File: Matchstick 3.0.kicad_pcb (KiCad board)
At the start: 2 copper layers, 60.2 x 34 mm, 11 parts, among them J3 Barrel_Jack, J4 Screw_Terminal_01x08, SW1 SparkFun_COM-08720, U3 M5StampS3

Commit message: updated sch+pcb
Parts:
- removed H1, H2: MountingHole, MountingHole:MountingHole_3.5mm
- removed U3: M5StampS3, M5Stack_SMD:M5StampS3
- added U1: M5StampS3, M5Stack_SMD:M5StampS3, B.Cu at (184.0, 107.5)
- J3: footprint Connector_Custom:BarrelJack_Horizontal_Custom -> Connector_BarrelJack:BarrelJack_Horizontal
- SW1: footprint Switch_SMD:SparkFun_COM-08720 -> SparkFun:SparkFun_COM-08720
- moved SW1 41.6 mm to (163.2, 95.1), turned to 90 degrees
- moved D1 26.5 mm to (168.6, 115.5)
- moved R1 26.5 mm to (165.6, 115.4)
- moved C2 26.3 mm to (179.9, 112.2), turned to 0 degrees
- moved J4 13.2 mm to (200.8, 116.8)
- moved C1 12.6 mm to (193.4, 105.4), turned to 180 degrees
- moved U2 12.1 mm to (193.3, 111.1), turned to 0 degrees
- moved J3 0.99 mm to (170.0, 104.5)
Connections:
- U2 pad 11: CLK2 -> CLK1
- U2 pad 3: CLK1 -> CLK2
- U2 pad 6: DATA1 -> DATA2
- U2 pad 8: DATA2 -> DATA1
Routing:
- net +5V: track 41.3 -> 106.2 mm
- net CLK2: track 1.75 -> 30.1 mm
- net GND: track 25.7 -> 45.7 mm, vias 0 -> 1
- net DATA2: track 2.02 -> 19.9 mm
- net unconnected-(D1-A-Pad2): track 1.78 -> 10.8 mm, vias 0 -> 1
- net C2: track 1.98 -> 10.9 mm, vias 0 -> 1
- net CLK1: track 14.5 -> 5.54 mm
- net C1: track 1.44 -> 9.07 mm, vias 0 -> 1
- net unconnected-(SW1-Pad1): track 28.2 -> 35.5 mm, vias 0 -> 1
- net D2: track 2.88 -> 9.55 mm, vias 0 -> 1
- net D1: track 2.11 -> 7.74 mm, vias 0 -> 1
- net DATA1: track 9.22 -> 5.67 mm
- removed copper zone on B.Cu, net GND
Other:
- board size 60.2 x 34 mm -> 47.2 x 34 mm

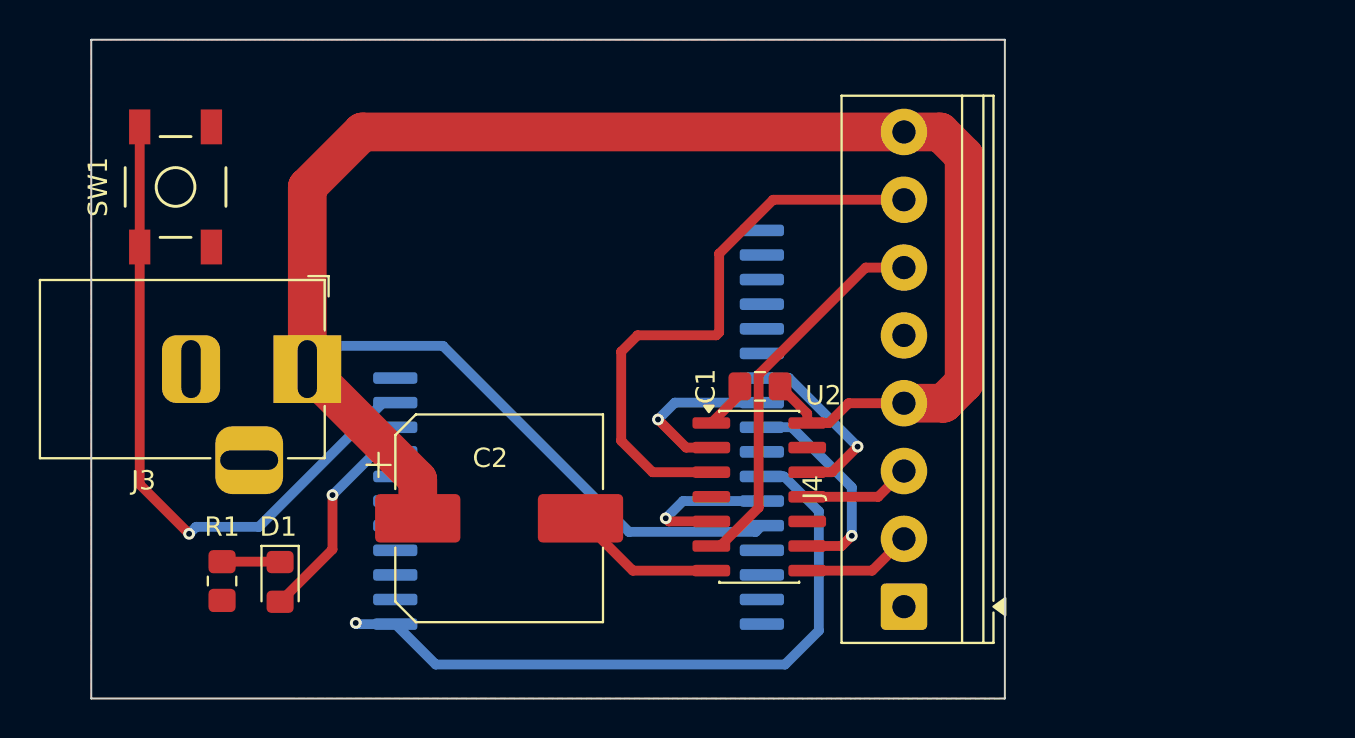
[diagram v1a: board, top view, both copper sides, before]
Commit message: fixed ground planes
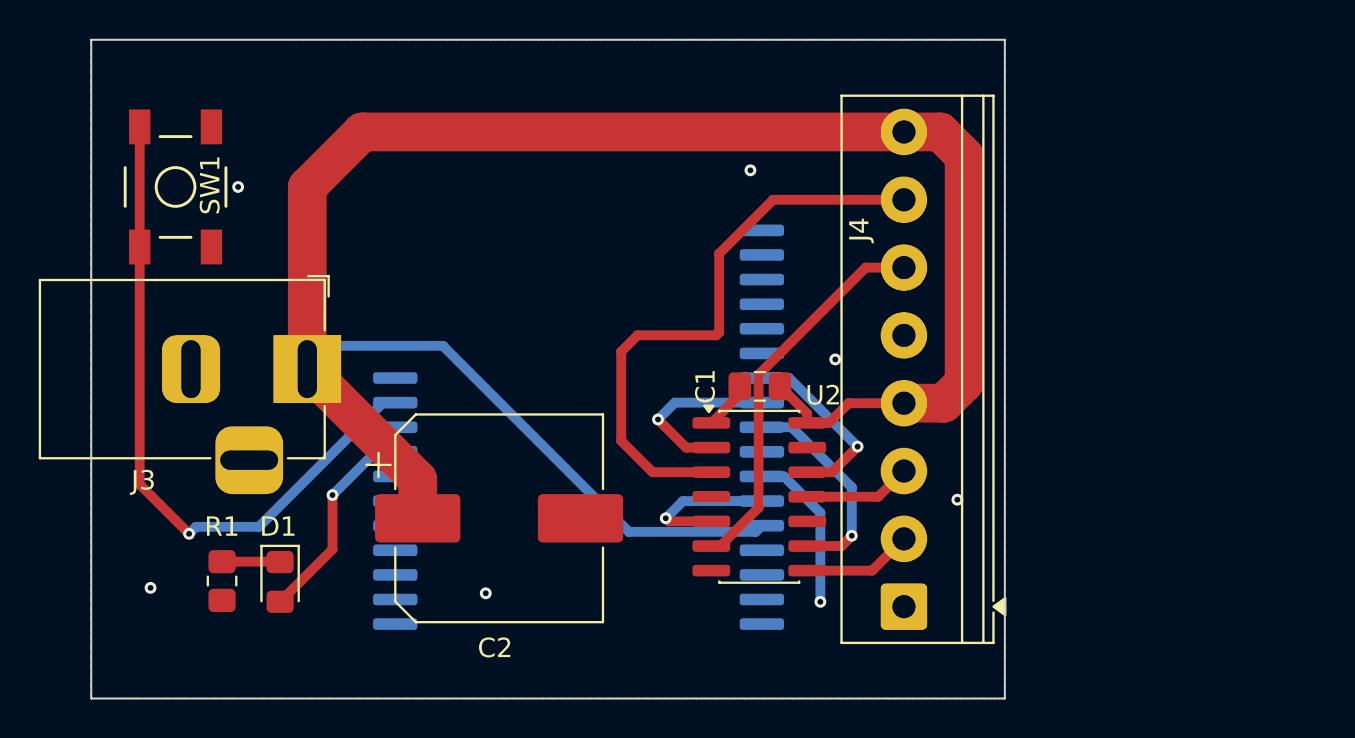
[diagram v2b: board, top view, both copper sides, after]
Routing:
- net GND: track 45.7 -> 10.9 mm, vias 1 -> 7
- added copper zone on B.Cu, net GND
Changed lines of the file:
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@@
 		(tags "THT Terminal Block Phoenix PT-1,5-8-3.5-H pitch 3.5mm size 28x7.6mm drill 1.2mm pad 2.4mm")
 		(property "Reference" "J4"
-			(at 6.16 -4.7 90)
+			(at 19.46 -2.292893 90)
 			(layer "F.SilkS")
 			(effects
@@
 		(tags "capacitor electrolytic")
 		(property "Reference" "C2"
-			(at -0.46 -3.11 0)
+			(at -0.2 6.7 0)
 			(layer "F.SilkS")
 			(effects
@@
 		(tags "Pushbutton Switch COM-08720")
 		(property "Reference" "SW1"
-			(at 0 -4 90)
+			(at 0.1 1.8 90)
 			(unlocked yes)
 			(layer "F.SilkS")
@@
 	)
 	(segment
-		(start 186.8 114.9)
-		(end 190.85 114.9)
-		(width 0.508)
-		(layer "F.Cu")
-		(net 2)
-	)
-	(segment
 		(start 192.325 105.39)
 		(end 192.325 105.805)
@@
 	)
 	(segment
-		(start 184.1 112.2)
-		(end 186.8 114.9)
-		(width 0.508)
-		(layer "F.Cu")
-		(net 2)
-	)
-	(segment
 		(start 192.325 105.805)
 		(end 190.85 107.28)
@@
 	)
 	(via
-		(at 172.5 117.6)
+		(at 192.87 94.24)
 		(size 0.61)
 		(drill 0.3)
 		(layers "F.Cu" "B.Cu")
+		(free yes)
 		(net 2)
 	)
-	(segment
-		(start 176.625 119.745)
-		(end 174.54 117.66)
+	(via
+		(at 196.48 116.51)
+		(size 0.61)
+		(drill 0.3)
+		(layers "F.Cu" "B.Cu")
+		(free yes)
+		(net 2)
+	)
+	(via
+		(at 197.25 104)
+		(size 0.61)
+		(drill 0.3)
+		(layers "F.Cu" "B.Cu")
+		(free yes)
+		(net 2)
+	)
+	(via
+		(at 203.55 111.24)
+		(size 0.61)
+		(drill 0.3)
+		(layers "F.Cu" "B.Cu")
+		(free yes)
+		(net 2)
+	)
+	(via
+		(at 179.21 116.07)
+		(size 0.61)
+		(drill 0.3)
+		(layers "F.Cu" "B.Cu")
+		(free yes)
+		(net 2)
+	)
+	(via
+		(at 161.91 115.79)
+		(size 0.61)
+		(drill 0.3)
+		(layers "F.Cu" "B.Cu")
+		(free yes)
+		(net 2)
+	)
+	(via
+		(at 166.43 95.1)
+		(size 0.61)
+		(drill 0.3)
+		(layers "F.Cu" "B.Cu")
+		(free yes)
+		(net 2)
+	)
+	(segment
+		(start 196.48 111.917001)
+		(end 196.48 116.51)
 		(width 0.508)
 		(layer "B.Cu")
@@
 	)
 	(segment
-		(start 196.4 111.837001)
-		(end 196.4 118)
+		(start 194.602999 110.04)
+		(end 196.48 111.917001)
 		(width 0.508)
 		(layer "B.Cu")
@@
 	)
 	(segment
-		(start 194.655 119.745)
-		(end 176.625 119.745)
-		(width 0.508)
-		(layer "B.Cu")
-		(net 2)
-	)
-	(segment
-		(start 194.602999 110.04)
-		(end 196.4 111.837001)
-		(width 0.508)
-		(layer "B.Cu")
-		(net 2)
-	)
-	(segment
 		(start 193.46 110.04)
 		(end 194.602999 110.04)
-		(width 0.508)
-		(layer "B.Cu")
-		(net 2)
-	)
-	(segment
-		(start 172.56 117.66)
-		(end 172.5 117.6)
-		(width 0.508)
-		(layer "B.Cu")
-		(net 2)
-	)
-	(segment
-		(start 196.4 118)
-		(end 194.655 119.745)
-		(width 0.508)
-		(layer "B.Cu")
-		(net 2)
-	)
-	(segment
-		(start 174.54 117.66)
-		(end 172.56 117.66)
 		(width 0.508)
 		(layer "B.Cu")
@@
 		(layer "F.Cu")
 		(hatch edge 0.5)
-		(priority 1)
 		(connect_pads
 			(clearance 0)
@@
 		(polygon
 			(pts
-				(xy 158.85 87.5) (xy 206 87.5) (xy 206 121.5) (xy 158.85 121.5)
+				(xy 158.85 87.5) (xy 158.85 121.5) (xy 205.998318 121.514769) (xy 205.998318 87.514769)
 			)
 		)
@@
 		(net 2)
 		(net_name "GND")
-		(layer "F.Cu")
+		(layers "F.Cu" "B.Cu")
 		(hatch edge 0.5)
+		(priority 1)
 		(connect_pads
-			(clearance 0)
+			(clearance 0.1)
 		)
 		(min_thickness 0.25)
@@
 		(polygon
 			(pts
-				(xy 158.85 87.5) (xy 158.85 121.5) (xy 205.998318 121.514769) (xy 205.998318 87.514769)
-			)
-		)
+				(xy 158.85 87.5) (xy 206 87.5) (xy 206 121.5) (xy 158.85 121.5)
+			)
+		)

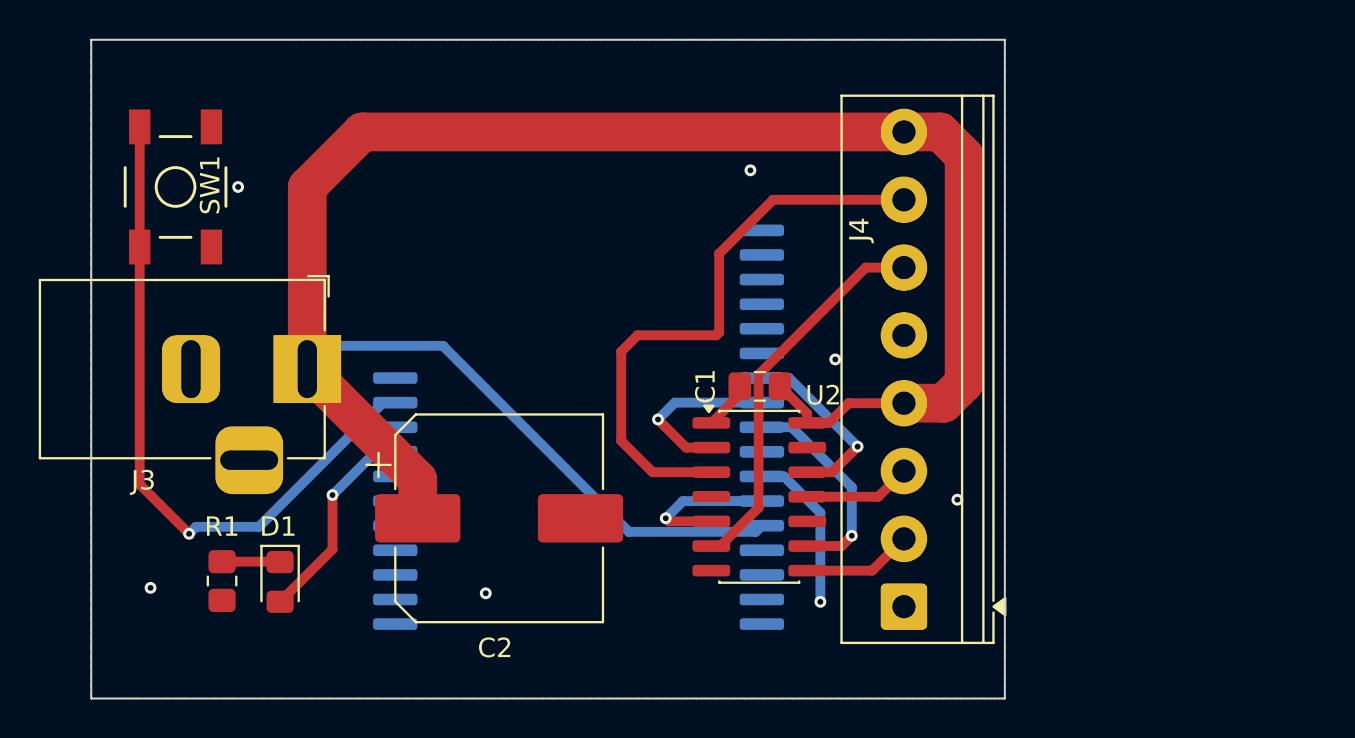
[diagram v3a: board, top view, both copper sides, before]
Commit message: fixed spacing and ERC and DRC errors
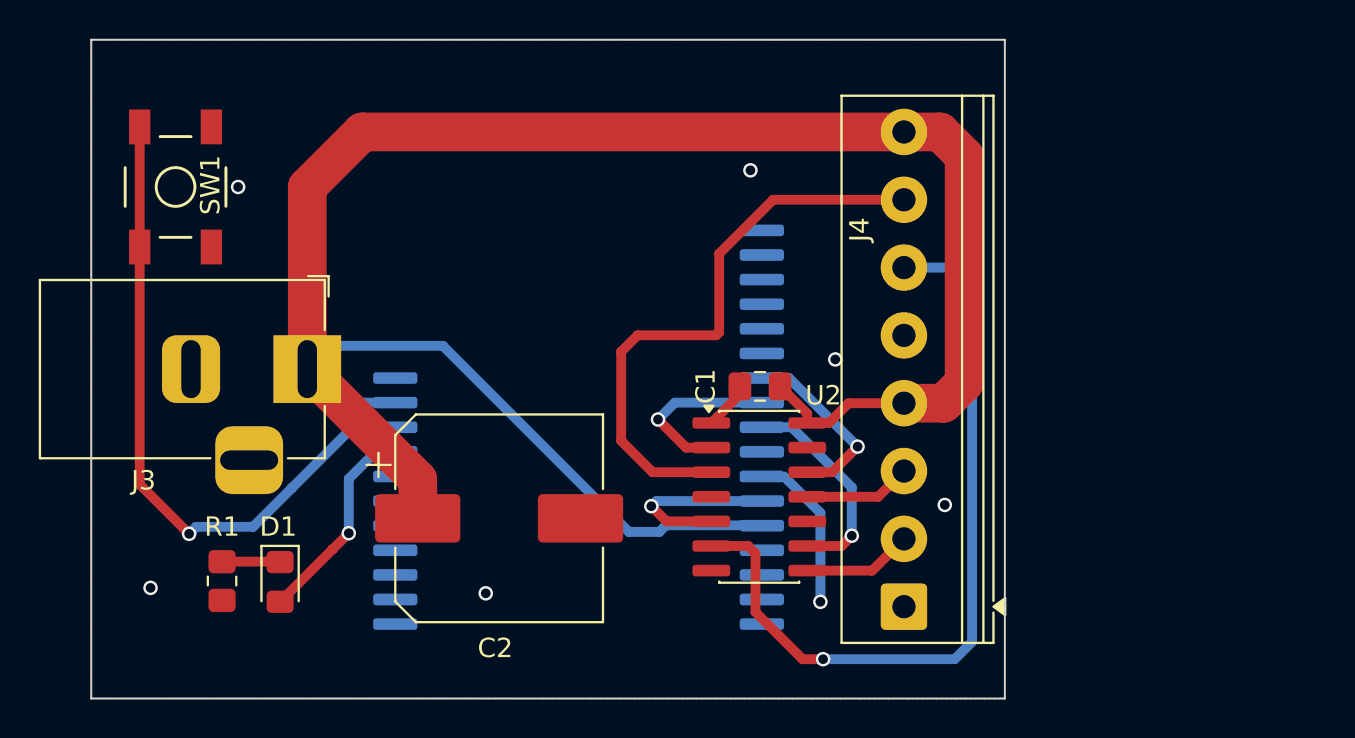
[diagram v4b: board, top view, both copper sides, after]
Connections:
- net Net-(D1-K) renamed /LED2
- D1 pad 2: unconnected-(D1-A-Pad2) -> /LED
- SW1 pad 1: unconnected-(SW1-Pad1) -> /SW1
- U1 pad 25: unconnected-(D1-A-Pad2) -> /LED
- U1 pad 27: unconnected-(SW1-Pad1) -> /SW1
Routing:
- net unconnected-(SW1-Pad1): track 35.5 -> 0.00 mm, vias 1 -> 0
- net /SW1: track 0.00 -> 35.0 mm, vias 0 -> 1
- net DATA2: track 19.9 -> 40.1 mm, vias 0 -> 1
- net /LED: track 0.00 -> 10.8 mm, vias 0 -> 1
- net unconnected-(D1-A-Pad2): track 10.8 -> 0.00 mm, vias 1 -> 0
- net D1: track 7.74 -> 9.23 mm
- net GND: track 10.9 -> 9.75 mm

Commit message: silkscreen logo
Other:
- board text added: "+5V +5V"
- board text added: "0x76656E Labs"
- board text added: "C1 G08"
- board text added: "C2 G09"
- board text added: "D1 G12"
- board text added: "D2 G07"
- board text added: "GND GND"
- board text added: "MATCH STICK 0x03"
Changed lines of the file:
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@@
 		(tags "capacitor handsolder")
 		(property "Reference" "C1"
-			(at 2.8 0 90)
+			(at 2.9325 0.06 180)
 			(layer "F.SilkS")
 			(effects
@@
 		(tags "SOIC SO")
 		(property "Reference" "U2"
-			(at 3.31 -5.23 0)
+			(at -2.015 5.61 0)
 			(layer "F.SilkS")
 			(effects
@@
 		(embedded_fonts no)
 	)
+	(gr_rect
+		(start 172.818554 87.57)
+		(end 194.451447 102.91)
+		(stroke
+			(width 0.15)
+			(type solid)
+		)
+		(fill yes)
+		(layer "F.SilkS")
+	)
 	(gr_line
 		(start 158.85 87.5)
@@
 		(layer "Edge.Cuts")
 	)
+	(gr_text "+5V     +5V"
+		(at 206.08 106.98 0)
+		(layer "B.SilkS" knockout)
+		(effects
+			(font
+				(size 1.25 1)
+				(thickness 0.15)
+				(bold yes)
+			)
+			(justify left bottom mirror)
+		)
+	)
+	(gr_text "C1       G08"
+		(at 206.03 110.54 0)
+		(layer "B.SilkS" knockout)
+		(effects
+			(font
+				(size 1.25 1)
+				(thickness 0.15)
+				(bold yes)
+			)
+			(justify left bottom mirror)
+		)
+	)
+	(gr_text "MATCH\nSTICK\n0x03"
+		(at 160.02 96.02 0)
+		(layer "B.SilkS" knockout)
+		(effects
+			(font
+				(size 1.5 1.5)
+				(thickness 0.375)
+				(bold yes)
+			)
+			(justify right bottom mirror)
+		)
+	)
+	(gr_text "GND     GND"
+		(at 206.05 103.55 0)
+		(layer "B.SilkS" knockout)
+		(effects
+			(font
+				(size 1.25 1)
+				(thickness 0.15)
+				(bold yes)
+			)
+			(justify left bottom mirror)
+		)
+	)
+	(gr_text "GND     GND"
+		(at 206.03 117.49 0)
+		(layer "B.SilkS" knockout)
+		(effects
+			(font
+				(size 1.25 1)
+				(thickness 0.15)
+				(bold yes)
+			)
+			(justify left bottom mirror)
+		)
+	)
+	(gr_text "D2       G07"
+		(at 206.1 100 0)
+		(layer "B.SilkS" knockout)
+		(effects
+			(font
+				(size 1.25 1)
+				(thickness 0.15)
+				(bold yes)
+			)
+			(justify left bottom mirror)
+		)
+	)
+	(gr_text "C2       G09\n"
+		(at 206.05 96.6 0)
+		(layer "B.SilkS" knockout)
+		(effects
+			(font
+				(size 1.25 1)
+				(thickness 0.15)
+				(bold yes)
+			)
+			(justify left bottom mirror)
+		)
+	)
+	(gr_text "D1       G12"
+		(at 206.08 113.95 0)
+		(layer "B.SilkS" knockout)
+		(effects
+			(font
+				(size 1.25 1)
+				(thickness 0.15)
+				(bold yes)
+			)
+			(justify left bottom mirror)
+		)
+	)
+	(gr_text "+5V     +5V"
+		(at 206.1 93.04 0)
+		(layer "B.SilkS" knockout)
+		(effects
+			(font
+				(size 1.25 1)
+				(thickness 0.15)
+				(bold yes)
+			)
+			(justify left bottom mirror)
+		)
+	)
+	(gr_text "0x76656E\nLabs"
+		(at 160.21 99.94 0)
+		(layer "B.SilkS")
+		(effects
+			(font
+				(size 1 0.98)
+				(thickness 0.15)
+				(bold yes)
+			)
+			(justify right bottom mirror)
+		)
+	)
 	(segment

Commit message: fixed the nets, and connections
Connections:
- U1 pad 12: D1 -> D2
- U1 pad 7: D2 -> C1
- U1 pad 8: C1 -> C2
- U1 pad 9: C2 -> D1
- U2 pad 12: D2 -> C1
- U2 pad 2: C1 -> C2
- U2 pad 5: D1 -> D2
- U2 pad 9: C2 -> D1
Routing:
- net C2: track 10.9 -> 9.07 mm
- net D1: track 9.23 -> 10.9 mm
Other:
- board text added: "C1 G07"
- board text added: "C2 G08"
- board text added: "D1 G09"
- board text added: "D2 G11"
- board text removed: "C1 G08"
- board text removed: "C2 G09"
- board text removed: "D1 G12"
- board text removed: "D2 G07"
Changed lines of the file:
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@@
 			(layers "F.Cu" "F.Mask" "F.Paste")
 			(roundrect_rratio 0.25)
-			(net 11 "C1")
+			(net 9 "C2")
 			(pinfunction "A")
 			(pintype "input")
@@
 			(layers "F.Cu" "F.Mask" "F.Paste")
 			(roundrect_rratio 0.25)
-			(net 8 "D1")
+			(net 10 "D2")
 			(pinfunction "A")
 			(pintype "input")
@@
 			(layers "F.Cu" "F.Mask" "F.Paste")
 			(roundrect_rratio 0.25)
-			(net 9 "C2")
+			(net 8 "D1")
 			(pinfunction "A")
 			(pintype "input")
@@
 			(layers "F.Cu" "F.Mask" "F.Paste")
 			(roundrect_rratio 0.25)
-			(net 10 "D2")
+			(net 11 "C1")
 			(pinfunction "A")
 			(pintype "input")
@@
 			(layers "B.Cu" "B.Mask" "B.Paste")
 			(roundrect_rratio 0.25)
-			(net 10 "D2")
+			(net 11 "C1")
 			(pinfunction "G7")
 			(pintype "bidirectional")
@@
 			(layers "B.Cu" "B.Mask" "B.Paste")
 			(roundrect_rratio 0.25)
-			(net 11 "C1")
+			(net 9 "C2")
 			(pinfunction "G8")
 			(pintype "bidirectional")
@@
 			(layers "B.Cu" "B.Mask" "B.Paste")
 			(roundrect_rratio 0.25)
-			(net 9 "C2")
+			(net 8 "D1")
 			(pinfunction "G9")
 			(pintype "bidirectional")
@@
 			(layers "B.Cu" "B.Mask" "B.Paste")
 			(roundrect_rratio 0.25)
-			(net 8 "D1")
+			(net 10 "D2")
 			(pinfunction "G11")
 			(pintype "bidirectional")
@@
 		(layer "F.SilkS")
 	)
+	(gr_rect
+		(start 160.25 89.07)
+		(end 167.43 99.49)
+		(stroke
+			(width 0.15)
+			(type default)
+		)
+		(fill no)
+		(layer "B.SilkS")
+	)
 	(gr_line
 		(start 158.85 87.5)
@@
 		)
 	)
-	(gr_text "C1       G08"
+	(gr_text "C1       G07"
 		(at 206.03 110.54 0)
 		(layer "B.SilkS" knockout)
@@
 		)
 	)
-	(gr_text "D2       G07"
+	(gr_text "D2       G11"
 		(at 206.1 100 0)
 		(layer "B.SilkS" knockout)
@@
 		)
 	)
-	(gr_text "C2       G09\n"
+	(gr_text "C2       G08\n"
 		(at 206.05 96.6 0)
 		(layer "B.SilkS" knockout)
@@
 		)
 	)
-	(gr_text "D1       G12"
+	(gr_text "D1       G09"
 		(at 206.08 113.95 0)
 		(layer "B.SilkS" knockout)
@@
 	)
 	(gr_text "0x76656E\nLabs"
-		(at 160.21 99.94 0)
+		(at 160.8 98.94 0)
 		(layer "B.SilkS")
 		(effects
 			(font
-				(size 1 0.98)
+				(size 0.8 0.8)
 				(thickness 0.15)
 				(bold yes)
@@
 	)
 	(segment
-		(start 187.755 111.575)
-		(end 188.54 112.36)
+		(start 197.57 113.63)
+		(end 198.1 113.1)
 		(width 0.508)
 		(layer "F.Cu")
@@
 	)
 	(segment
-		(start 188.54 112.36)
-		(end 190.85 112.36)
+		(start 195.8 113.63)
+		(end 197.57 113.63)
 		(width 0.508)
 		(layer "F.Cu")
@@
 	)
 	(via
-		(at 187.755 111.575)
+		(at 198.1 113.1)
 		(size 0.75)
 		(drill 0.5)
@@
 	)
 	(segment
-		(start 188.02 111.31)
-		(end 193.46 111.31)
+		(start 195 107.5)
+		(end 193.46 107.5)
 		(width 0.508)
 		(layer "B.Cu")
@@
 	)
 	(segment
-		(start 187.755 111.575)
-		(end 188.02 111.31)
+		(start 198.1 110.6)
+		(end 195 107.5)
 		(width 0.508)
 		(layer "B.Cu")
@@
 	)
 	(segment
-		(start 197.57 113.63)
-		(end 198.1 113.1)
+		(start 198.1 113.1)
+		(end 198.1 110.6)
+		(width 0.508)
+		(layer "B.Cu")
+		(net 8)
+	)
+	(segment
+		(start 189.55 108.55)
+		(end 188.1 107.1)
 		(width 0.508)
 		(layer "F.Cu")
@@
 	)
 	(segment
-		(start 195.8 113.63)
-		(end 197.57 113.63)
+		(start 190.85 108.55)
+		(end 189.55 108.55)
 		(width 0.508)
 		(layer "F.Cu")
@@
 	)
 	(via
-		(at 198.1 113.1)
+		(at 188.1 107.1)
 		(size 0.75)
 		(drill 0.5)
@@
 	)
 	(segment
-		(start 195 107.5)
-		(end 193.46 107.5)
-		(width 0.508)
-		(layer "B.Cu")
-		(net 9)
-	)
-	(segment
-		(start 198.1 110.6)
-		(end 195 107.5)
+		(start 188.97 106.23)
+		(end 193.46 106.23)
 		(width 0.508)
 		(layer "B.Cu")
@@
 	)
 	(segment
-		(start 198.1 113.1)
-		(end 198.1 110.6)
+		(start 188.1 107.1)
+		(end 188.97 106.23)
 		(width 0.508)
 		(layer "B.Cu")
@@
 	)
 	(segment
-		(start 197.08 109.82)
-		(end 198.4 108.5)
+		(start 187.755 111.575)
+		(end 188.54 112.36)
 		(width 0.508)
 		(layer "F.Cu")
@@
 	)
 	(segment
-		(start 195.8 109.82)
-		(end 197.08 109.82)
+		(start 188.54 112.36)
+		(end 190.85 112.36)
 		(width 0.508)
 		(layer "F.Cu")
@@
 	)
 	(via
-		(at 198.4 108.5)
+		(at 187.755 111.575)
 		(size 0.75)
 		(drill 0.5)
@@
 	)
 	(segment
-		(start 194.86 104.96)
-		(end 193.46 104.96)
+		(start 188.02 111.31)
+		(end 193.46 111.31)
 		(width 0.508)
 		(layer "B.Cu")
@@
 	)
 	(segment
-		(start 198.4 108.5)
-		(end 194.86 104.96)
+		(start 187.755 111.575)
+		(end 188.02 111.31)
 		(width 0.508)
 		(layer "B.Cu")
@@
 	)
 	(segment
-		(start 189.55 108.55)
-		(end 188.1 107.1)
+		(start 197.08 109.82)
+		(end 198.4 108.5)
 		(width 0.508)
 		(layer "F.Cu")
@@
 	)
 	(segment
-		(start 190.85 108.55)
-		(end 189.55 108.55)
+		(start 195.8 109.82)
+		(end 197.08 109.82)
 		(width 0.508)
 		(layer "F.Cu")
@@
 	)
 	(via
-		(at 188.1 107.1)
+		(at 198.4 108.5)
 		(size 0.75)
 		(drill 0.5)
@@
 	)
 	(segment
-		(start 188.97 106.23)
-		(end 193.46 106.23)
+		(start 194.86 104.96)
+		(end 193.46 104.96)
 		(width 0.508)
 		(layer "B.Cu")
@@
 	)
 	(segment
-		(start 188.1 107.1)
-		(end 188.97 106.23)
+		(start 198.4 108.5)
+		(end 194.86 104.96)
 		(width 0.508)
 		(layer "B.Cu")
@@
 		)
 	)
+	(group ""
+		(members "0e220948-0c99-46df-8c10-0e8a88680065" "2eb774eb-ed1f-4744-ad87-57a9c581328a"
+			"f99b8019-54df-44b1-b5f7-fb0933b396bf"
+		)
+	)
